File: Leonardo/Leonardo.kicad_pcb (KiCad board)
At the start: 2 copper layers, 68.5 x 53.4 mm, 53 parts, among them J1 Power, J2 Analog, J3 Digital_2, J4 Digital_1, J5 ISP, J6 USB_Micro, J7 Barrel_Jack, Q1 FDN340P, SW1 TL3342, U1 LMV358IDGKR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

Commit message: Tidy up a few things
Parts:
- F1: footprint Fuse_Holders_and_Fuses:Fuse_SMD1206_Reflow -> MF-MSMF050-2..:FUSC4632X85N
- moved F1 1.59 mm to (78.0, 97.0)
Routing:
- net /USB_IN: track 6.08 -> 8.91 mm
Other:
- board text added: "D13"
- board text added: "ISP"
- board text added: "Pwr"
- board text added: "Rx"
- board text added: "Tx"

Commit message: More tidy-up and silk screen
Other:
- board text added: "+3V3"
- board text added: "+5V"
- board text added: "A0"
- board text added: "A1"
- board text added: "A2"
- board text added: "A3"
- board text added: "A4"
- board text added: "A5"
- board text added: "AREF"
- board text added: "D0"
- board text added: "D1"
- board text added: "D10"
- board text added: "D11"
- board text added: "D12"
- board text added: "D2"
- board text added: "D3"
- board text added: "D4"
- board text added: "D5"
- board text added: "D6"
- board text added: "D7"
- board text added: "D8"
- board text added: "D9"
- board text added: "GND"
- board text added: "Reset"
- board text added: "SCL"
- board text added: "SDA"
- board text added: "VIN"
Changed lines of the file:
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@@
   (general
     (links 138)
-    (no_connects 1)
+    (no_connects 0)
     (area 71.069999 73.571526 139.720001 127.050001)
     (thickness 1.6)
-    (drawings 80)
+    (drawings 112)
     (tracks 825)
     (zones 0)
@@
     (tags SOT-23)
     (attr smd)
-    (fp_text reference Q1 (at 0 -2.5) (layer F.SilkS)
+    (fp_text reference Q1 (at 1.889 -1.397) (layer F.SilkS)
       (effects (font (size 1 1) (thickness 0.15)))
     )
@@
     (tags "SPST Tactile Switch")
     (attr smd)
-    (fp_text reference SW1 (at 0 -3.75) (layer F.SilkS)
+    (fp_text reference SW1 (at 0.127 0) (layer F.SilkS) hide
       (effects (font (size 1 1) (thickness 0.15)))
     )
@@
       (net 20 /USB_IN))
   )
+  (gr_text +5V (at 101.6 122.809 90) (layer F.SilkS)
+    (effects (font (size 1 1) (thickness 0.2)) (justify left))
+  )
+  (gr_text Reset (at 104.013 122.809 90) (layer F.SilkS)
+    (effects (font (size 1 1) (thickness 0.2)) (justify left))
+  )
+  (gr_text +3V3 (at 106.68 122.809 90) (layer F.SilkS)
+    (effects (font (size 1 1) (thickness 0.2)) (justify left))
+  )
+  (gr_text +5V (at 109.22 122.809 90) (layer F.SilkS)
+    (effects (font (size 1 1) (thickness 0.2)) (justify left))
+  )
+  (gr_text GND (at 111.76 122.809 90) (layer F.SilkS)
+    (effects (font (size 1 1) (thickness 0.2)) (justify left))
+  )
+  (gr_text GND (at 114.3 122.809 90) (layer F.SilkS)
+    (effects (font (size 1 1) (thickness 0.2)) (justify left))
+  )
+  (gr_text VIN (at 116.84 122.809 90) (layer F.SilkS)
+    (effects (font (size 1 1) (thickness 0.2)) (justify left))
+  )
+  (gr_text A5 (at 134.62 122.809 90) (layer F.SilkS)
+    (effects (font (size 1 1) (thickness 0.2)) (justify left))
+  )
+  (gr_text A4 (at 132.08 122.809 90) (layer F.SilkS)
+    (effects (font (size 1 1) (thickness 0.2)) (justify left))
+  )
+  (gr_text A3 (at 129.54 122.809 90) (layer F.SilkS)
+    (effects (font (size 1 1) (thickness 0.2)) (justify left))
+  )
+  (gr_text A2 (at 127 122.809 90) (layer F.SilkS)
+    (effects (font (size 1 1) (thickness 0.2)) (justify left))
+  )
+  (gr_text A1 (at 124.46 122.809 90) (layer F.SilkS)
+    (effects (font (size 1 1) (thickness 0.2)) (justify left))
+  )
+  (gr_text A0 (at 121.92 122.809 90) (layer F.SilkS)
+    (effects (font (size 1 1) (thickness 0.2)) (justify left))
+  )
+  (gr_text D0 (at 134.62 77.851 90) (layer F.SilkS)
+    (effects (font (size 1 1) (thickness 0.2)) (justify right))
+  )
+  (gr_text D1 (at 132.08 77.851 90) (layer F.SilkS)
+    (effects (font (size 1 1) (thickness 0.2)) (justify right))
+  )
+  (gr_text D2 (at 129.54 77.851 90) (layer F.SilkS)
+    (effects (font (size 1 1) (thickness 0.2)) (justify right))
+  )
+  (gr_text D3 (at 127 77.851 90) (layer F.SilkS)
+    (effects (font (size 1 1) (thickness 0.2)) (justify right))
+  )
+  (gr_text D4 (at 124.46 77.851 90) (layer F.SilkS)
+    (effects (font (size 1 1) (thickness 0.2)) (justify right))
+  )
+  (gr_text D5 (at 121.92 77.851 90) (layer F.SilkS)
+    (effects (font (size 1 1) (thickness 0.2)) (justify right))
+  )
+  (gr_text D6 (at 119.38 77.851 90) (layer F.SilkS)
+    (effects (font (size 1 1) (thickness 0.2)) (justify right))
+  )
+  (gr_text D7 (at 116.84 77.851 90) (layer F.SilkS)
+    (effects (font (size 1 1) (thickness 0.2)) (justify right))
+  )
+  (gr_text D8 (at 112.776 77.851 90) (layer F.SilkS)
+    (effects (font (size 1 1) (thickness 0.2)) (justify right))
+  )
+  (gr_text D9 (at 110.236 77.851 90) (layer F.SilkS)
+    (effects (font (size 1 1) (thickness 0.2)) (justify right))
+  )
+  (gr_text D10 (at 107.696 77.851 90) (layer F.SilkS)
+    (effects (font (size 1 1) (thickness 0.2)) (justify right))
+  )
+  (gr_text D11 (at 105.156 77.851 90) (layer F.SilkS)
+    (effects (font (size 1 1) (thickness 0.2)) (justify right))
+  )
+  (gr_text D12 (at 102.616 77.851 90) (layer F.SilkS)
+    (effects (font (size 1 1) (thickness 0.2)) (justify right))
+  )
+  (gr_text D13 (at 100.076 77.851 90) (layer F.SilkS)
+    (effects (font (size 1 1) (thickness 0.2)) (justify right))
+  )
+  (gr_text GND (at 97.536 77.851 90) (layer F.SilkS)
+    (effects (font (size 1 1) (thickness 0.2)) (justify right))
+  )
+  (gr_text AREF (at 94.996 77.851 90) (layer F.SilkS)
+    (effects (font (size 1 1) (thickness 0.2)) (justify right))
+  )
+  (gr_text SDA (at 92.456 77.851 90) (layer F.SilkS)
+    (effects (font (size 1 1) (thickness 0.2)) (justify right))
+  )
+  (gr_text SCL (at 89.916 77.851 90) (layer F.SilkS)
+    (effects (font (size 1 1) (thickness 0.2)) (justify right))
+  )
+  (gr_text Reset (at 76.327 75.057) (layer F.SilkS)
+    (effects (font (size 1.2 1.2) (thickness 0.2)))
+  )
   (gr_text D13 (at 71.755 86.36 270) (layer F.SilkS)

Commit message: rLab logo and info on the back
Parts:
- added G***: LOGO, rLab:RLAB_LOGO, B.Cu at (128.8, 113.5)
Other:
- board text added: "Board Stupid Leonardo - v1.0"
- board text added: "http://rlab.org.uk/"

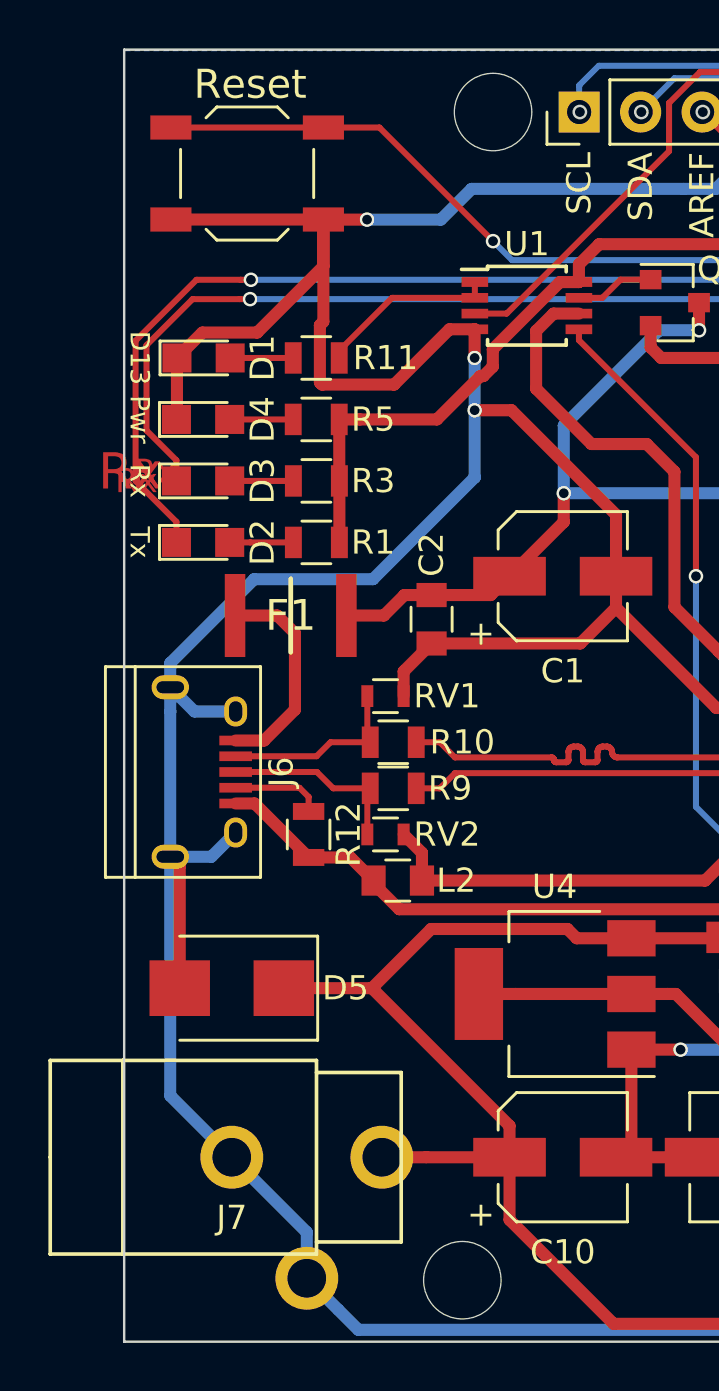
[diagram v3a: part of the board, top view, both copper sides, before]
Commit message: Added a bit of heat dissipation for the +5V regulator
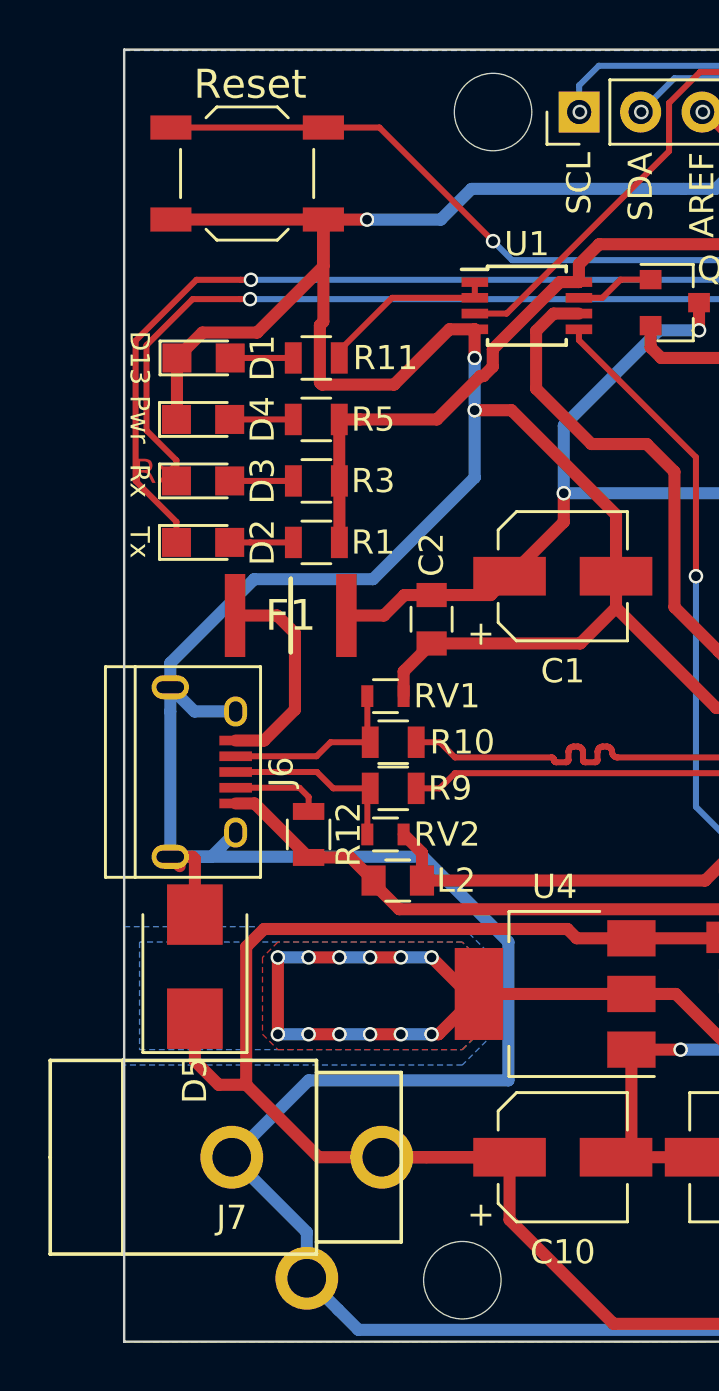
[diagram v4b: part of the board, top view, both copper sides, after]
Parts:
- moved D5 1.76 mm to (74.0, 111.5), turned to 90 degrees
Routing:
- net +5V: track 191.9 -> 213.0 mm, vias 1 -> 13
- net GND: track 375.6 -> 394.3 mm
- net /VIN: track 68.8 -> 82.4 mm
- added copper zone on B.Cu, net +5V
- added copper zone on F.Cu, net +5V

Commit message: More tidy up
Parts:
- moved C1 0.59 mm to (89.8, 95.4)
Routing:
- net GND: track 394.3 -> 398.5 mm
- net /TXLED: track 63.2 -> 64.2 mm
- net /RXLED: track 74.9 -> 75.9 mm
- net +5V: track 213.0 -> 214.0 mm
- net Net-(R11-Pad1): track 7.46 -> 8.44 mm
- net VBUS: track 101.5 -> 100.7 mm

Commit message: More tidy up
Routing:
- net GND: track 398.5 -> 388.2 mm
- net VBUS: track 100.7 -> 102.9 mm
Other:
- outline, holes or cut-outs redrawn
- net class Default: clearance 0.2 -> 0.16
- net class Power: clearance 0.2 -> 0.16
- rule trace_clearance: 0.2 -> 0.16
